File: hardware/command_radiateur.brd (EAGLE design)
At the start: 136.4 x 73.5 mm, 32 parts, among them IC2 3.3V, Q1 8MHz, X2 B1

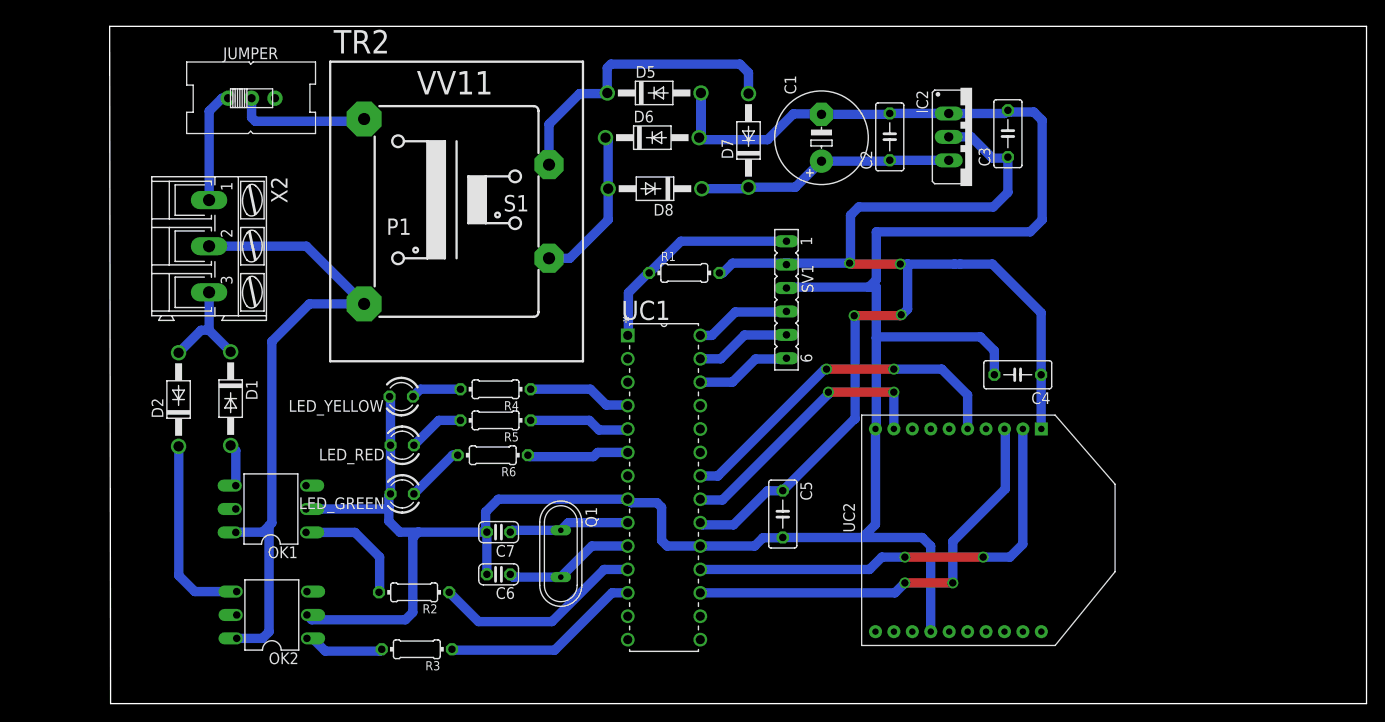
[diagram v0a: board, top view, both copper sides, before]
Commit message: update PCB size, insert hole to insert into G368 box
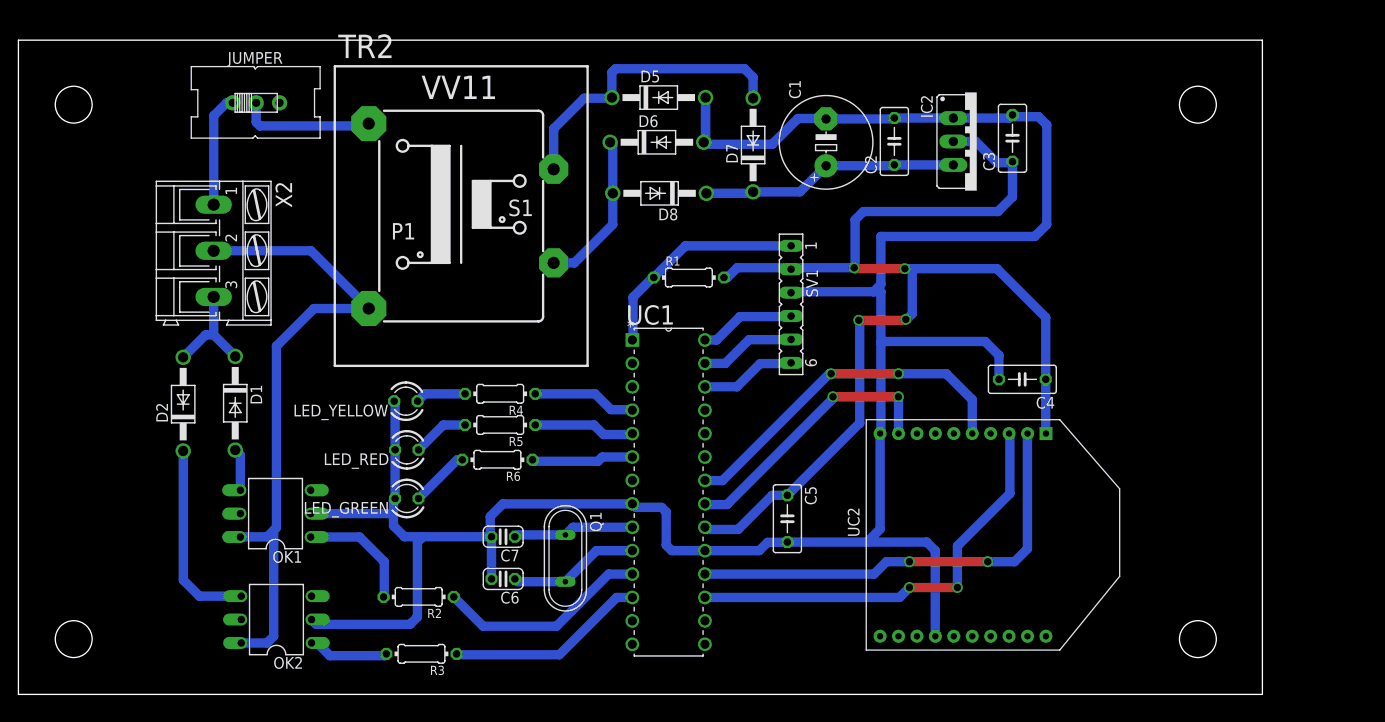
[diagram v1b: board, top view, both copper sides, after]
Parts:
- moved C1 0.71 mm to (77.7, 60.9)
- moved C2 0.71 mm to (85.1, 61.0)
- moved C3 0.71 mm to (97.9, 61.4)
- moved C4 0.71 mm to (99.0, 35.2)
- moved C5 0.71 mm to (73.5, 20.1)
- moved C6 0.71 mm to (42.6, 13.5)
- moved C7 0.71 mm to (42.6, 18.1)
- moved D1 0.71 mm to (13.5, 32.6)
- moved D2 0.71 mm to (7.88, 32.5)
- moved D5 0.71 mm to (59.5, 65.8)
- moved D6 0.71 mm to (59.3, 60.9)
- moved D7 0.71 mm to (69.7, 60.6)
- moved D8 0.71 mm to (59.6, 55.4)
- moved IC2 0.71 mm to (94.0, 61.0)
- moved JUMPER 0.71 mm to (15.8, 65.2)
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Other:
- board size 136.4 x 73.5 mm -> 135 x 71 mm
